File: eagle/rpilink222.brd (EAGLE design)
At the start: 84.8 x 55.9 mm, 62 parts, among them IC1 IMS-C011M2S20E, IC2 MCP23017SO, IC3 SM77H, IC4 '244, IC5 MAX3467EPA, IC6 MAX3467EPA, IC7 MAX3467EPA, X1 RASPI_BOARD_AB_E2P

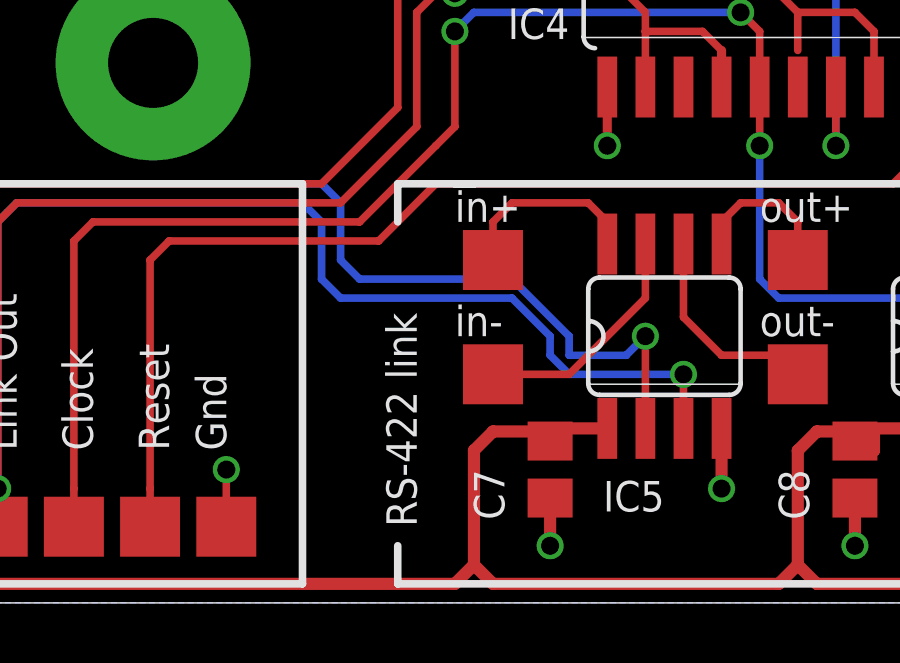
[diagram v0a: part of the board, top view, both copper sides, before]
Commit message: Added component values, added rs-422 bias resistors.
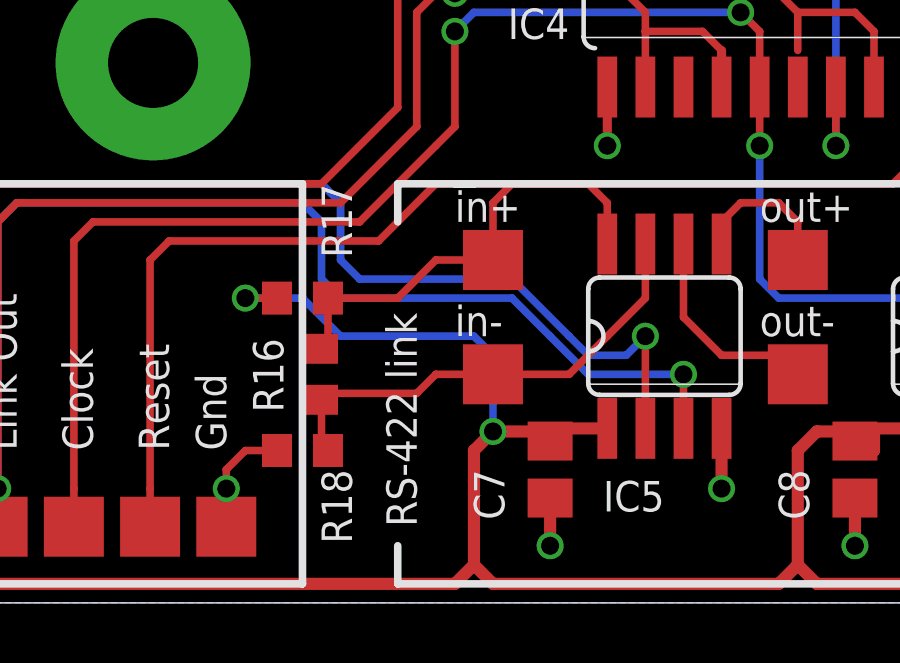
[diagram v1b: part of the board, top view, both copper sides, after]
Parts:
- added R16: 120R, rcl:R0603
- added R17, R18: 1k, rcl:R0603
- C1, C2, C3, C6, C7, C8, C9: value (none) -> 100n
- C4: value (none) -> 10µ/16v
- C5: value (none) -> 1µ
- R1, R2, R3, R4, R5, R6: value (none) -> 1k
- R10, R11, R15, R7, R8, R9: value (none) -> 6k8
- R12: value (none) -> 5k6
- R13, R14: value (none) -> 120R
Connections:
- net 5V0: now also R17.2
- net GND: now also R18.2
- net IN+: now also R16.2, R17.1
- net IN-: now also R16.1, R18.1
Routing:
- net 5V0: track 312.3 -> 324.9 mm, vias 5 -> 7
- net IN+: track 6.34 -> 15.4 mm
- net IN-: track 7.94 -> 15.8 mm
- net GND: track 88.6 -> 90.6 mm

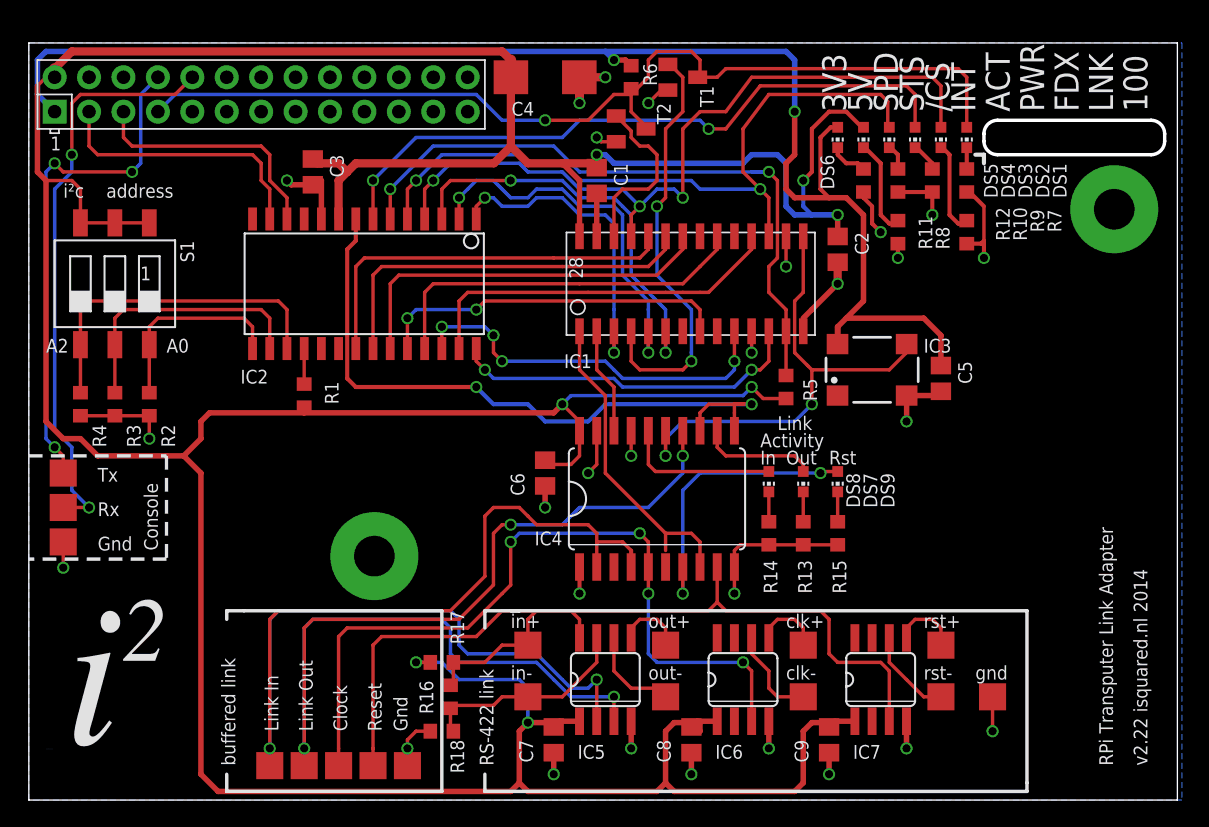
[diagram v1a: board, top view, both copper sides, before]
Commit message: usb cut-out
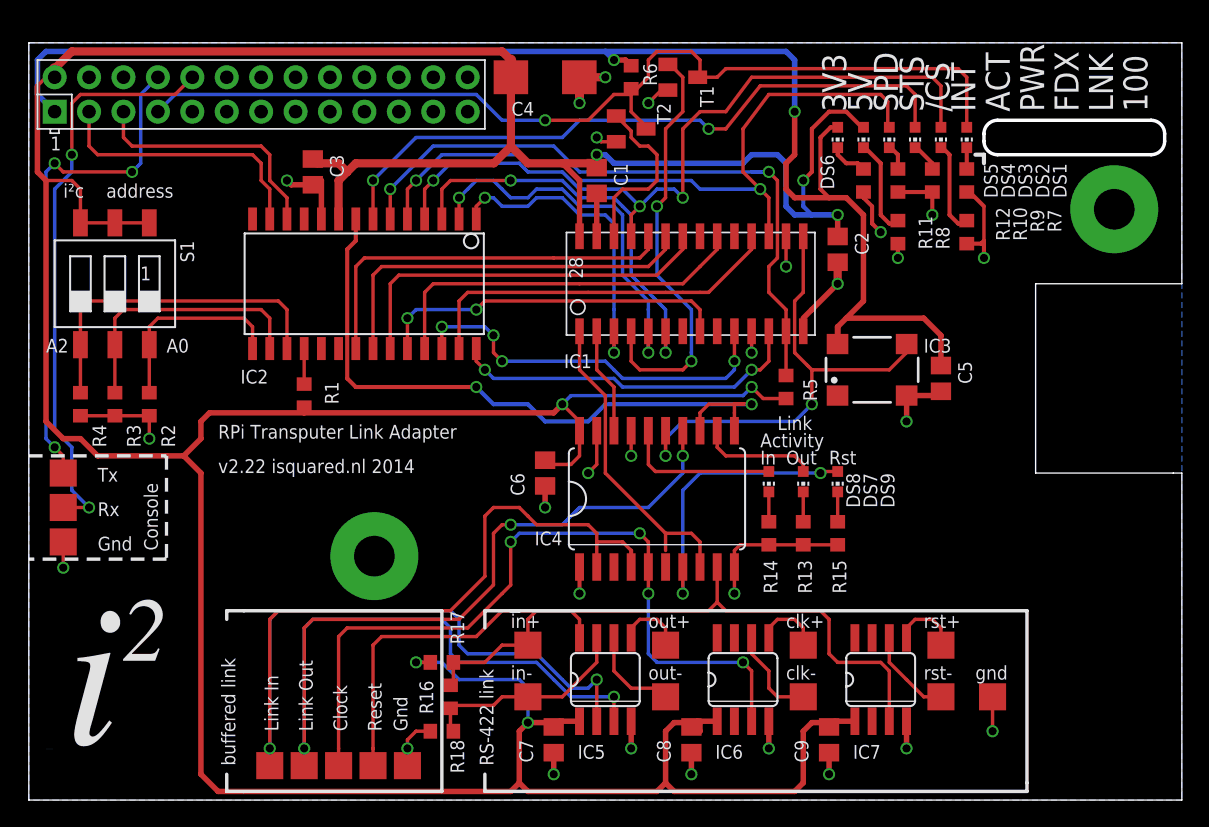
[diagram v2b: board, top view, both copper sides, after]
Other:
- board size 84.8 x 55.9 mm -> 85.1 x 55.9 mm
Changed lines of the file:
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@@
 <board>
 <plain>
-<wire x1="0" y1="0" x2="84.76" y2="0" width="0" layer="20"/>
-<wire x1="84.76" y1="0" x2="84.76" y2="55.87" width="0" layer="20"/>
-<wire x1="84.76" y1="55.87" x2="0" y2="55.87" width="0" layer="20"/>
 <wire x1="0" y1="55.87" x2="0" y2="0" width="0" layer="20"/>
 <text x="2.54" y="44.45" size="1.016" layer="25">i²c</text>
@@
 <text x="26.035" y="5.08" size="1.016" layer="25" rot="R90">Reset</text>
 <text x="27.94" y="5.08" size="1.016" layer="25" rot="R90">Gnd</text>
-<text x="80.01" y="2.54" size="1.016" layer="21" rot="R90">RPi Transputer Link Adapter</text>
-<text x="82.55" y="2.54" size="1.016" layer="21" rot="R90">v2.22 isquared.nl 2014</text>
+<text x="13.97" y="26.67" size="1.016" layer="21">RPi Transputer Link Adapter</text>
+<text x="13.97" y="24.13" size="1.016" layer="21">v2.22 isquared.nl 2014</text>
 <wire x1="0" y1="25.4" x2="10.16" y2="25.4" width="0.254" layer="21" style="shortdash"/>
 <wire x1="10.16" y1="25.4" x2="10.16" y2="17.78" width="0.254" layer="21" style="shortdash"/>
@@
 <wire x1="33.655" y1="13.97" x2="33.655" y2="12.7" width="0.254" layer="21"/>
 <wire x1="33.655" y1="0.635" x2="33.655" y2="1.905" width="0.254" layer="21"/>
+<wire x1="85.09" y1="38.1" x2="74.295" y2="38.1" width="0" layer="20"/>
+<wire x1="74.295" y1="38.1" x2="74.295" y2="24.13" width="0" layer="20"/>
+<wire x1="74.295" y1="24.13" x2="84.455" y2="24.13" width="0" layer="20"/>
+<wire x1="84.455" y1="24.13" x2="85.09" y2="24.13" width="0" layer="20"/>
+<wire x1="85.09" y1="38.1" x2="85.09" y2="55.88" width="0" layer="20"/>
+<wire x1="85.09" y1="24.13" x2="85.09" y2="0" width="0" layer="20"/>
+<wire x1="85.09" y1="55.88" x2="0" y2="55.88" width="0" layer="20"/>
+<wire x1="85.09" y1="0" x2="0" y2="0" width="0" layer="20"/>
 </plain>
 <attributes>
